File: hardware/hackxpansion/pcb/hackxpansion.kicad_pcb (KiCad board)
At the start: 4 copper layers, 52 x 69 mm, 103 parts, among them CN1 533981471, CN2 533981471, CN3 533981471, CN4 533981471, IC1 ADS7128IRTET, J2 USB_C_Receptacle_USB2.0_14P, J3 Conn_ARM_JTAG_SWD_10, Q1 BSS138, Q2 2N7002, SW1 SW_Push, SW2 SW_Push, SW3 SW_On_Off, U2 RP2354B, U5 SPX3819M5-L-3-3, U7 BQ24075RGT, U8 USBLC6-2SC6, Y1 ABM8-272-T3

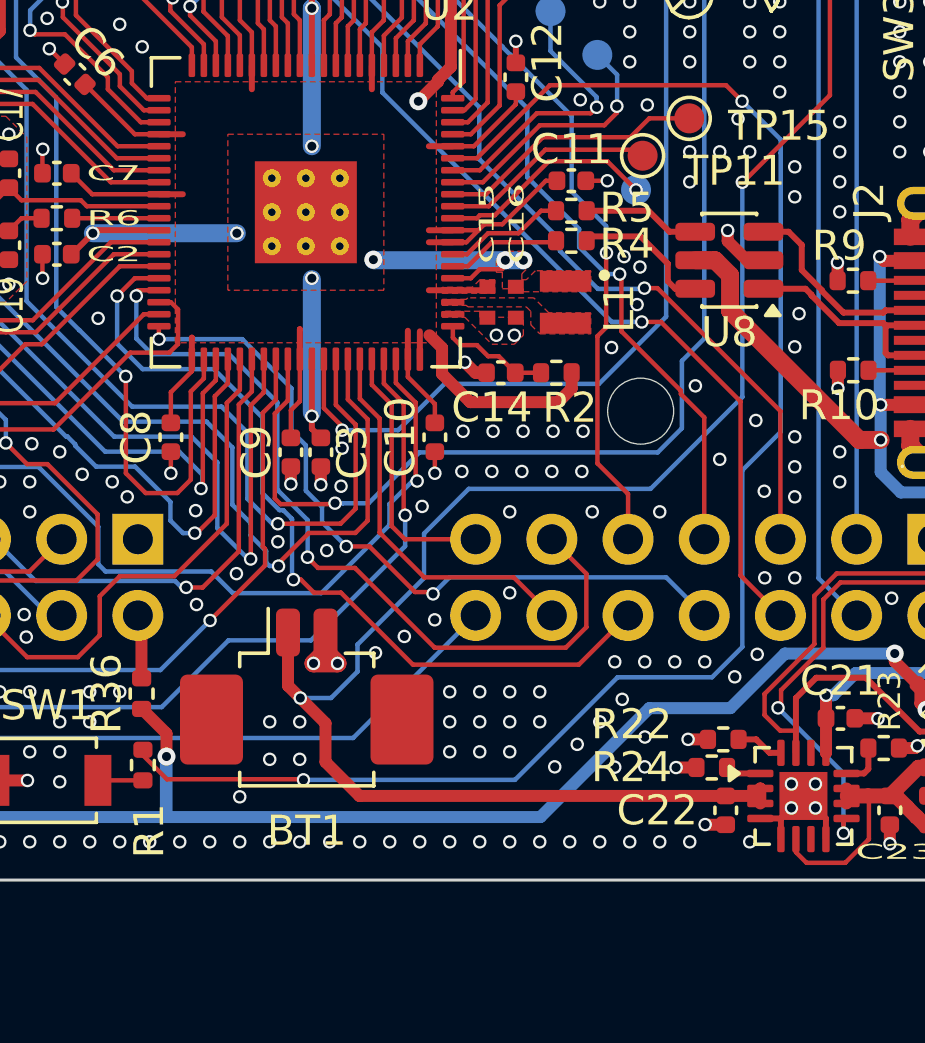
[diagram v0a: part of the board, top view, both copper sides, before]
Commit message: replaced battery connector with test pads
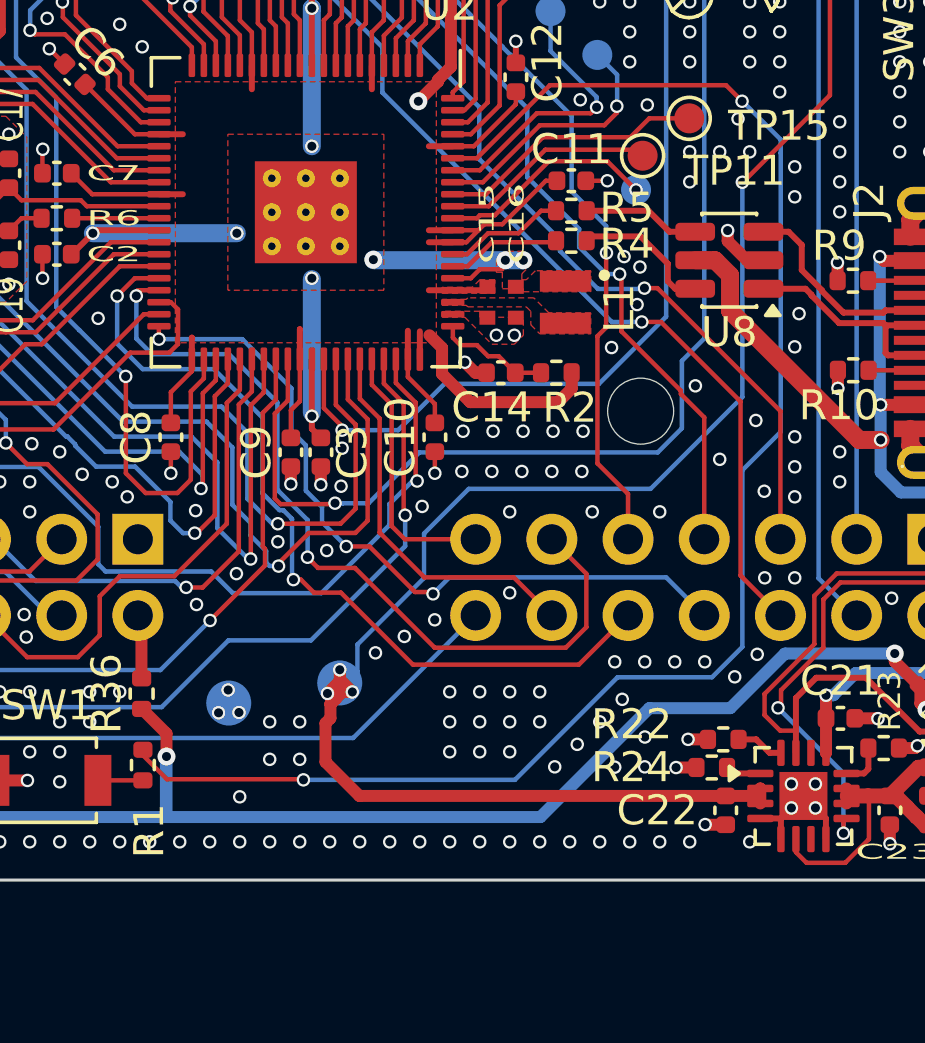
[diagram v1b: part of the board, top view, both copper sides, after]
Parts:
- removed BT1: Battery_Cell, Connector_Molex:Molex_PicoBlade_53261-0271_1x02-1MP_P1.25mm_Horizontal
- added BAT+: TestPoint, TestPoint:TestPoint_Pad_D1.5mm, B.Cu at (129.0, 94.3)
- added GND: TestPoint, TestPoint:TestPoint_Pad_D1.5mm, B.Cu at (125.3, 95.0)
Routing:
- net /GND: track 63.1 -> 60.5 mm, vias 416 -> 417
- net /Main Board/Power/+BATT: track 59.6 -> 60.3 mm, vias 2 -> 4
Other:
- board text added: "Credits: - Simon - Hack Club - KiCAD discord - r/PrintedCircuitBoard"
- board text removed: "Mentions: - Simon - Hack Club - KiCAD discord - r/PrintedCircuitBoard"

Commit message: added more vias, and repaced 100k with 10k
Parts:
- moved R15 1.14 mm to (147.1, 69.7)
- moved TP12 0.64 mm to (135.4, 72.1)
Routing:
- net Net-(SW3A-C): track 1.42 -> 2.56 mm
- net /GND: track 60.5 -> 59.5 mm, vias 417 -> 486
- net /Main Board/Power/+BATT: track 60.3 -> 59.4 mm
- net /DAUGHT_GND: vias 203 -> 204

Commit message: pcb: fixed warnings
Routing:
- net /+3V3: track 300.2 -> 299.8 mm, vias 17 -> 16

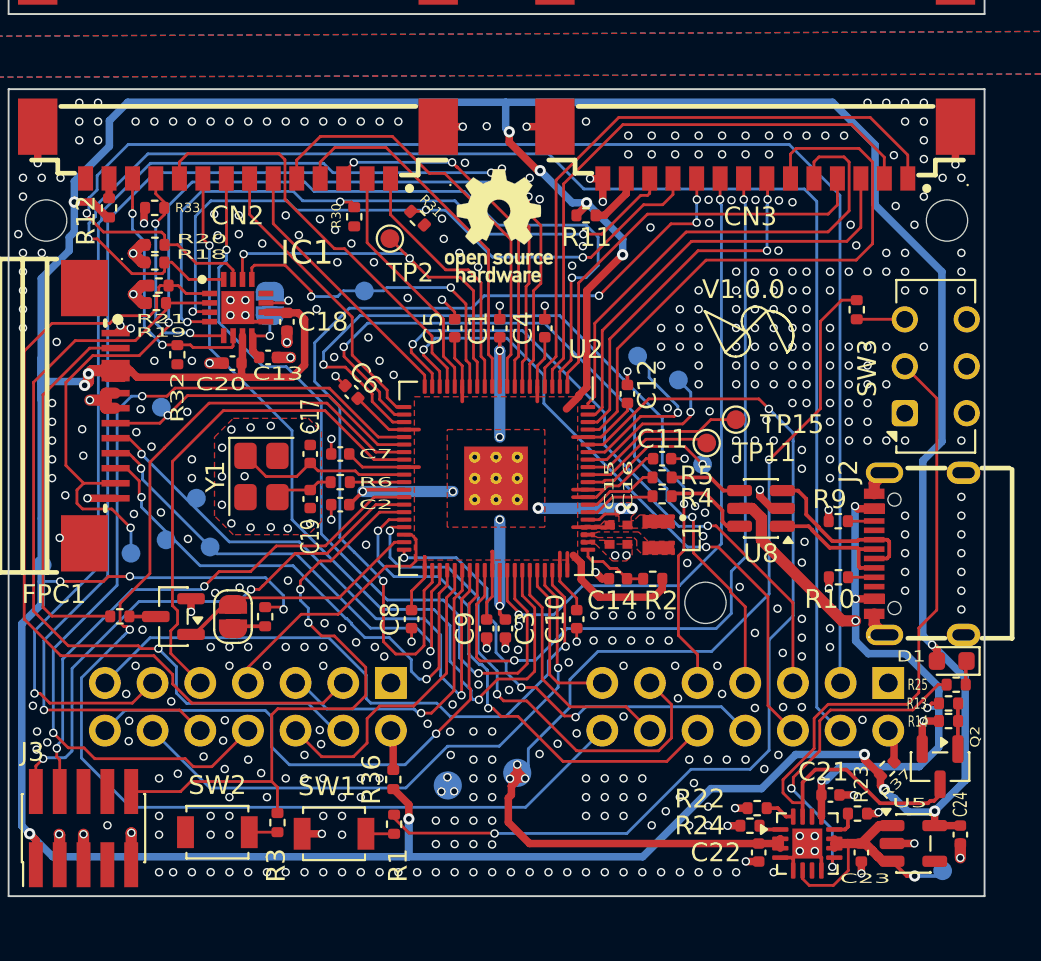
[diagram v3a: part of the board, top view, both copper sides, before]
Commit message: pcb: more vias, shortened bat+ trace
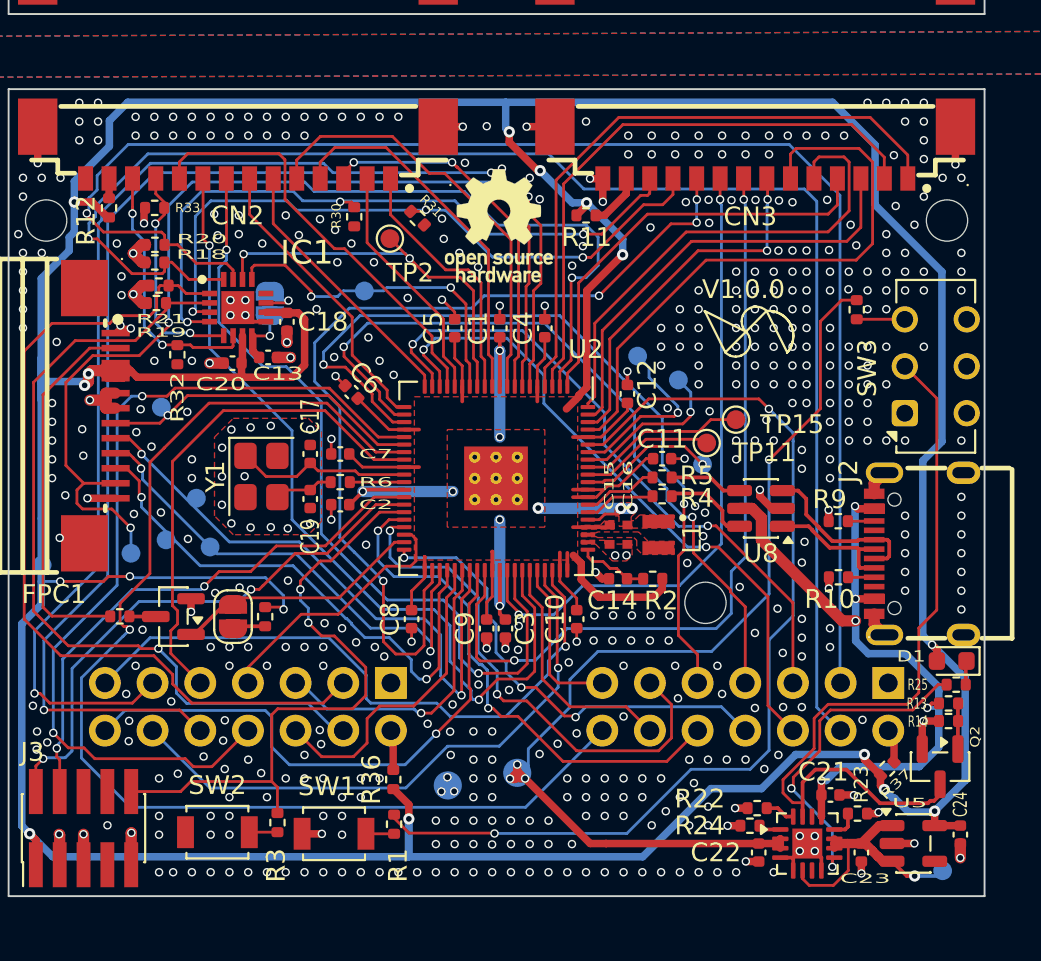
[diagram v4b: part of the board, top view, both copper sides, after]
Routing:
- net /Main Board/Power/+BATT: track 59.4 -> 56.5 mm
- net /GND: vias 486 -> 521
